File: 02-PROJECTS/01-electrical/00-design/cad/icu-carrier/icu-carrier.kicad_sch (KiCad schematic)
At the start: 109 parts, among them J1 DT13-06PA, J2 backlight out, J3 DT13-12PA, J4 BT817 EVE bridge header, J5 Teensy 4.1 socket - 2 x 24 fe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, Q1 SQD50P06 class, >= 60 V, Q2 MMBT3904, SW1 IC22, U1 LMR36015FSCQ-Q1, U2 VN5E class, >= 6 A - DNP, U3 TCAN1042HVDRQ1, U4 LM393, U5 74LVC1G17, U7 LSM6DSO / ICM-42688-P, U8 XIAO ESP32C3

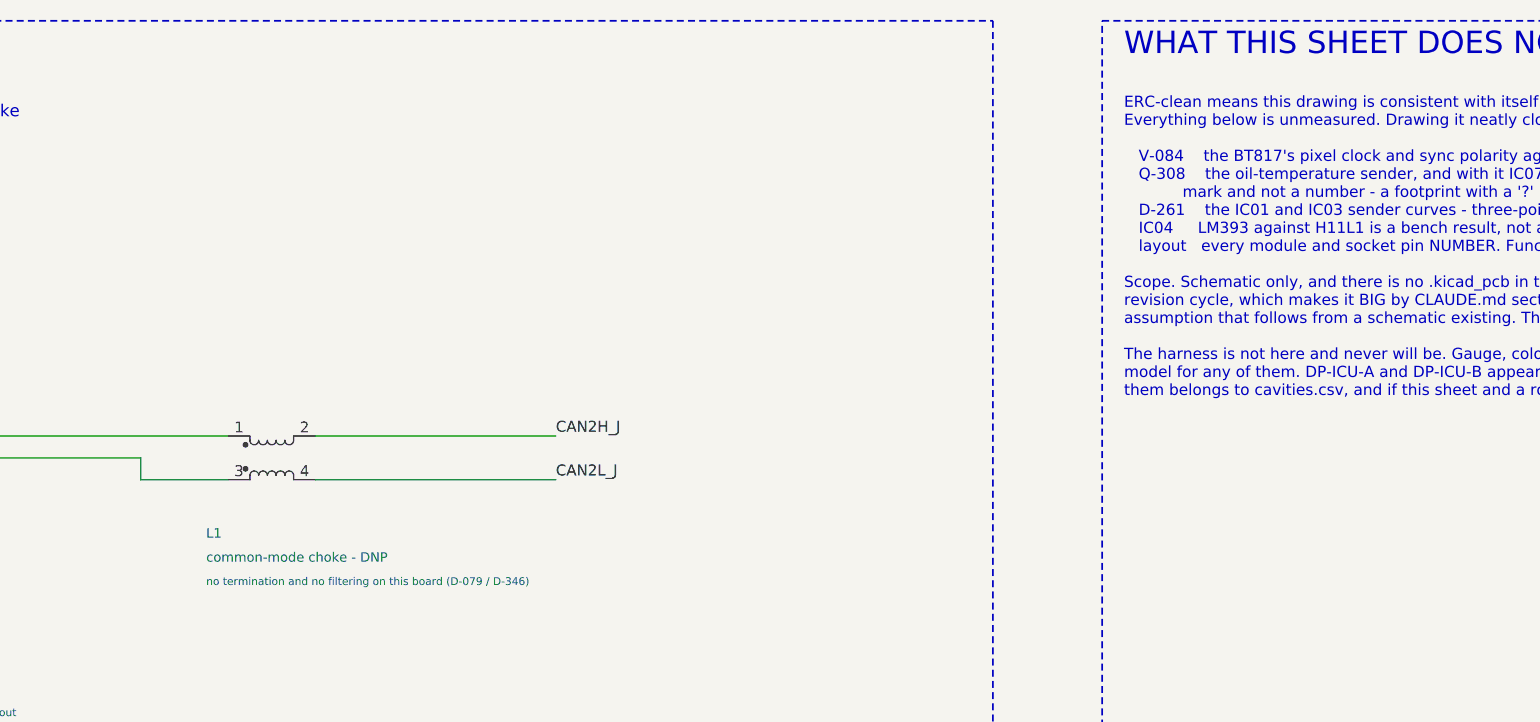
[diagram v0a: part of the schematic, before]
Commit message: ICU carrier: 0 Ω links across the DNP CAN choke (D-452)
L1 sits in series between U3 and J1 and is marked DNP, so as drawn CANH and
CANL were open between the transceiver and the drop. R44 and R45 (0 Ω, 0805)
now bridge it, the same as the DCU sheet. L1 is flagged DNP, with its reason
in the value. ERC is 0 errors and 0 warnings. F9's note tells the layout to
pull the two parts in with Update PCB from Schematic.

Co-Authored-By: Claude Opus 5.5 <noreply@anthropic.com>
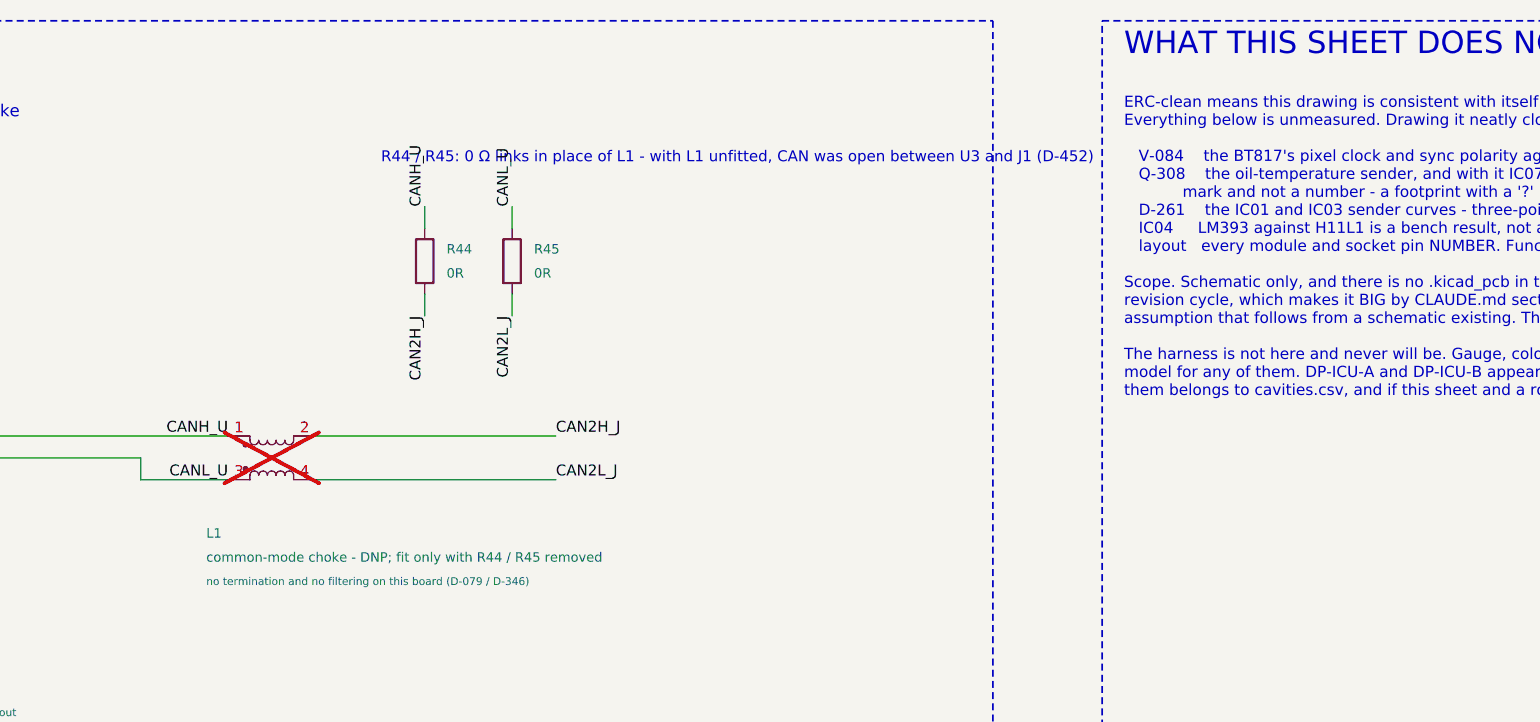
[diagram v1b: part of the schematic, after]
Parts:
- added R44, R45: 0R, Resistor_SMD:R_0805_2012Metric, symbol icu-carrier:R
- L1: value common-mode choke - DNP -> common-mode choke - DNP; fit only with R44 / R45 removed; now not fitted
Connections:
- net CAN2H_J: now also R44.2
- net CAN2L_J: now also R45.2
- net CANH_U: now reaches L1.1, U3.7 (CANH)
- net CANH_U: now also R44.1
- net CANL_U: now reaches L1.3, U3.6 (CANL)
- net CANL_U: now also R45.1
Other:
- note added: "R44 / R45: 0 Ω links in place of L1 - with L1 unfitted, CAN was open between U3 and J1 (D-452)"
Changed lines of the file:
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@@
 		(on_board yes)
 		(in_pos_files yes)
-		(dnp no)
+		(dnp yes)
 		(property "Reference" "L1"
 			(at 505.46 72.26 0)
@@
 			)
 		)
-		(property "Value" "common-mode choke - DNP"
+		(property "Value" "common-mode choke - DNP; fit only with R44 / R45 removed"
 			(at 505.46 75.06 0)
 			(show_name no)
@@
 	(junction (at 119.3800 111.7600) (diameter 0) (color 0 0 0 0)
 	)
+	(symbol
+		(lib_id "icu-carrier:R")
+		(at 530.86 40.64 0)
+		(unit 1)
+		(body_style 1)
+		(exclude_from_sim no)
+		(in_bom yes)
+		(on_board yes)
+		(in_pos_files yes)
+		(dnp no)
+		(property "Reference" "R44"
+			(at 533.4 39.24 0)
+			(show_name no)
+			(do_not_autoplace no)
+			(effects
+				(font
+					(size 1.1 1.1)
+				)
+				(justify left)
+			)
+		)
+		(property "Value" "0R"
+			(at 533.4 42.04 0)
+			(show_name no)
+			(do_not_autoplace no)
+			(effects
+				(font
+					(size 1.1 1.1)
+				)
+				(justify left)
+			)
+		)
+		(property "Footprint" "Resistor_SMD:R_0805_2012Metric"
+			(at 530.86 40.64 0)
+			(hide yes)
+			(show_name no)
+			(do_not_autoplace no)
+			(effects
+				(font
+					(size 1.27 1.27)
+				)
+			)
+		)
+		(property "Datasheet" ""
+			(at 530.86 40.64 0)
+			(show_name no)
+			(do_not_autoplace no)
+			(effects
+				(font
+					(size 1.27 1.27)
+				)
+			)
+		)
+		(property "Description" ""
+			(at 530.86 40.64 0)
+			(show_name no)
+			(do_not_autoplace no)
+			(effects
+				(font
+					(size 1.27 1.27)
+				)
+			)
+		)
+		(pin "1"
+		)
+		(pin "2"
+		)
+		(instances
+			(project "icu-carrier"
+				(path "/c75d3432-4fb5-46c2-a0c1-15c6416c4dd0"
+					(reference "R44")
+					(unit 1)
+				)
+			)
+		)
+	)
+	(wire (pts (xy 530.86 36.83) (xy 530.86 34.29))
+		(stroke (width 0) (type default))
+	)
+	(label "CANH_U"
+		(at 530.86 34.29 90)
+		(effects
+			(font
+				(size 1.27 1.27)
+			)
+			(justify left bottom)
+		)
+	)
+	(wire (pts (xy 530.86 44.45) (xy 530.86 46.99))
+		(stroke (width 0) (type default))
+	)
+	(label "CAN2H_J"
+		(at 530.86 46.99 270)
+		(effects
+			(font
+				(size 1.27 1.27)
+			)
+			(justify right bottom)
+		)
+	)
+	(symbol
+		(lib_id "icu-carrier:R")
+		(at 541.02 40.64 0)
+		(unit 1)
+		(body_style 1)
+		(exclude_from_sim no)
+		(in_bom yes)
+		(on_board yes)
+		(in_pos_files yes)
+		(dnp no)
+		(property "Reference" "R45"
+			(at 543.56 39.24 0)
+			(show_name no)
+			(do_not_autoplace no)
+			(effects
+				(font
+					(size 1.1 1.1)
+				)
+				(justify left)
+			)
+		)
+		(property "Value" "0R"
+			(at 543.56 42.04 0)
+			(show_name no)
+			(do_not_autoplace no)
+			(effects
+				(font
+					(size 1.1 1.1)
+				)
+				(justify left)
+			)
+		)
+		(property "Footprint" "Resistor_SMD:R_0805_2012Metric"
+			(at 541.02 40.64 0)
+			(hide yes)
+			(show_name no)
+			(do_not_autoplace no)
+			(effects
+				(font
+					(size 1.27 1.27)
+				)
+			)
+		)
+		(property "Datasheet" ""
+			(at 541.02 40.64 0)
+			(show_name no)
+			(do_not_autoplace no)
+			(effects
+				(font
+					(size 1.27 1.27)
+				)
+			)
+		)
+		(property "Description" ""
+			(at 541.02 40.64 0)
+			(show_name no)
+			(do_not_autoplace no)
+			(effects
+				(font
+					(size 1.27 1.27)
+				)
+			)
+		)
+		(pin "1"
+		)
+		(pin "2"
+		)
+		(instances
+			(project "icu-carrier"
+				(path "/c75d3432-4fb5-46c2-a0c1-15c6416c4dd0"
+					(reference "R45")
+					(unit 1)
+				)
+			)
+		)
+	)
+	(wire (pts (xy 541.02 36.83) (xy 541.02 34.29))
+		(stroke (width 0) (type default))
+	)
+	(label "CANL_U"
+		(at 541.02 34.29 90)
+		(effects
+			(font
+				(size 1.27 1.27)
+			)
+			(justify left bottom)
+		)
+	)
+	(wire (pts (xy 541.02 44.45) (xy 541.02 46.99))
+		(stroke (width 0) (type default))
+	)
+	(label "CAN2L_J"
+		(at 541.02 46.99 270)
+		(effects
+			(font
+				(size 1.27 1.27)
+			)
+			(justify right bottom)
+		)
+	)
+	(label "CANH_U"
+		(at 508 60.96 180)
+		(effects
+			(font
+				(size 1.27 1.27)
+			)
+			(justify right bottom)
+		)
+	)
+	(label "CANL_U"
+		(at 508 66.04 180)
+		(effects
+			(font
+				(size 1.27 1.27)
+			)
+			(justify right bottom)
+		)
+	)
+	(text "R44 / R45: 0 Ω links in place of L1 - with L1 unfitted, CAN was open between U3 and J1 (D-452)"
+		(exclude_from_sim no)
+		(at 525.78 27.94 0)
+		(effects
+			(font
+				(size 1.27 1.27)
+			)
+			(justify left top)
+		)
+	)
 	(sheet_instances

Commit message: Electrical: the ICU carrier's provisional board - placed, routed, poured, DRC clean, 3D complete, STEP built (F9, F10)
110 x 80 mm provisional outline (confirm until C4 / F11); DT13-06PA / 12PA footprints from TE 114-151046; the XIAO on castellations 1-14 in 1x7 sockets, EN as a P-FET power-cycle; freerouting plus a grid router, 0 unrouted; GND poured both sides; DRC 0/0/0, ERC 0/0, check.py 0 mismatches; every footprint modelled, vendor models through RX7_MODELS. Parts P169 / P109 / P176, IC24, CK25; rows F9, F10.

Co-Authored-By: Claude Fable 5.1 <noreply@anthropic.com>
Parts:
- removed J4: BT817 EVE bridge header, Connector_PinHeader_2.54mm:PinHeader_1x10_P2.54mm_Vertical, symbol icu-carrier:BT817_HDR
- removed U7: LSM6DSO / ICM-42688-P, Connector_PinHeader_2.54mm:PinHeader_1x06_P2.54mm_Vertical, symbol icu-carrier:IMU_6DOF
- added J4: ME817EV CN8 - 2x8 host header, JP1 2-3 (5 V from 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, Connector_PinSocket_2.54mm:PinSocket_2x08_P2.54mm_Vertical, symbol icu-carrier:BT817_CN8
- added Q3: DMG3415U class P-FET, SOT-23 - confirm, Package_TO_SOT_SMD:SOT-23, symbol icu-carrier:Q_PMOS_GSD
- added Q4: MMBT3904, Package_TO_SOT_SMD:SOT-23, symbol icu-carrier:MMBT3904
- added R46, R47: 10k, Resistor_SMD:R_0805_2012Metric, symbol icu-carrier:R
- added U7: Adafruit 4517 LSM6DSOX+LIS3MDL (LSM6DSO class, P1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, icu-carrier:IMU_Adafruit_4517_Socket, symbol icu-carrier:IMU_4517
- J1: footprint Connector_PinHeader_2.54mm:PinHeader_2x03_P2.54mm_Vertical -> icu-carrier:DT13-06PA
- J3: footprint Connector_PinHeader_2.54mm:PinHeader_2x06_P2.54mm_Vertical -> icu-carrier:DT13-12PA
- U2: now not fitted
- U3, U4: footprint Package_SO:JEITA_SOIC-8_3.9x4.9mm_P1.27mm -> Package_SO:SOIC-8_3.9x4.9mm_P1.27mm
- U8: value XIAO ESP32C3 -> XIAO ESP32C3 2x7 socket (Seeed, S-490); footprint RF_Module:MCU_Seeed_ESP32C3 -> icu-carrier:XIAO_ESP32C3_Socket_2x07; Note IC24 - its OWN 3.3 V LDO (D-273) -> IC24 - its OWN 3.3 V LDO (D-273), in two 1x7 sockets. Back 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
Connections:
- net +3V3: now also U7.1 (VIN)
- net +5V: now also J4.10 (5V_HOST), Q3.2 (S), R46.1; no longer C19.1, U8.1 (5V)
- net BT817_INT: now also J4.14 (INT)
- net BT817_PD: now also J4.13 (PD)
- net BT_IO2: now also J4.6 (QSPI_IO2)
- net BT_IO3: now also J4.5 (QSPI_IO3)
- net GND: now also U8.13 (GND), J4.11 (GND), J4.12 (GND), Q4.2 (E), U7.3 (GND); no longer U8.2 (GND)
- net I2C_SCL: now also U7.4 (SCL)
- net I2C_SDA: now also U7.5 (SDA)
- net IMU_INT: now also U7.11 (INT1)
- net RADIO_BOOT: now also U8.10 (D9/MISO); no longer U8.7 (BOOT)
- net RADIO_EN: now also R47.1; no longer U8.6 (EN)
- net RADIO_RX: now also U8.8 (D7/RX); no longer U8.5 (RX)
- net RADIO_TX: now also U8.7 (D6/TX); no longer U8.4 (TX)
- net SPI_CS: now also J4.2 (QSPI_CS)
- net SPI_MISO: now also J4.3 (QSPI_IO1)
- net SPI_MOSI: now also J4.4 (QSPI_IO0)
- net SPI_SCK: now also J4.1 (QSPI_SCK)
- new net: Q3.1 (G), Q4.3 (C), R46.2
- new net: Q4.1 (B), R47.2
- new net RADIO_5V: C19.1, Q3.3 (D), U8.14 (VBUS)
- no-connect marks 9 -> 27
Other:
- note added: "IC24. The module sits in two 1x7 sockets so it can be swapped (D-273: its own LDO; a BLE scan peaks near 300 mA). EN 34 cannot reach the ESP32-C3's CHIP_EN - on the XIAO it is only back pad 17 (TP6, S-490) - so the Teensy power-cycles the module instead: EN high turns Q4 on, Q4 pulls Q3's gate low, Q3 passes +5V to VBUS (R46 holds it OFF when the Teensy is in reset). BOOT 35 holds D9 / GPIO9 low 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"
- note added: "The Teensy is drawn as the SOCKET it plugs into and nothing more. Pad n = Teensy 4.1 edge pin n (pad 1 = GND at the USB end, 25-48 up the right side): the record assigns every pin in icu_channels.teensy_pin (D-377) and cad/check.py holds this sheet to it, pin by pin. The 8 MB PSRAM (APS6404L-3SQR) is not on this sheet - it solders to the Teensy's own underside pads, not to the carrier. Nothing ta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"
- note removed: "The Teensy is drawn as the SOCKET it plugs into and nothing more. The reason is R11 and CONVENTIONS section 2.8: the record assigns no Teensy pin numbers anywhere. icu_channels says 'ADC', 'digital, input capture', 'QSPI header', 'I2C', 'Serial2 + 2 GPIO' - and stops. Drawing a pinout would put facts on this sheet that the record does not have, and a schematic that quietly picks an answer is wors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"
- note removed: "The antenna end overhangs the board edge with a 5 mm keep-out toward an RF-transparent enclosure wall (D-265's edge rule becomes D-270's face rule). Scan the advertisement always; open FFE1 only when cell detail is wanted; never write. FEE7 and any DFU characteristic are never touched - that is the door to a bricked pack (D-330, D-345)."
